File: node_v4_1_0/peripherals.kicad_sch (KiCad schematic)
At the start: 28 parts, among them J3 Conn_Coaxial, U10 MCP7940 / DS1307 / PCF8523, U11 1042240820, U12 CAT24M01W, U13 MAX31342EWA+T, U6 RFM69HCW, U9 SIM7080G

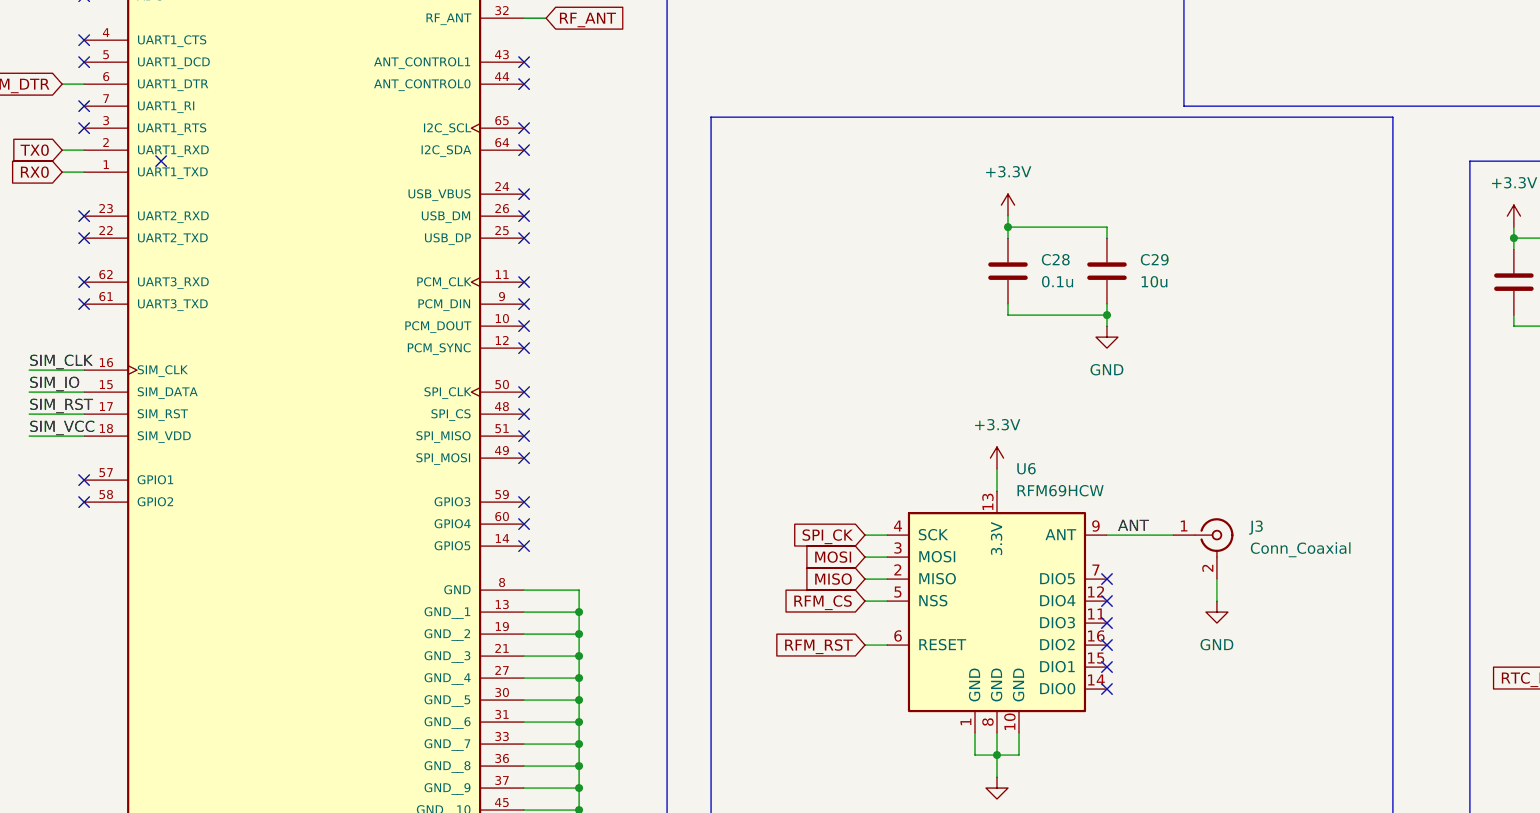
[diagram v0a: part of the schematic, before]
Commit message: small changes to 4.1.1 routing
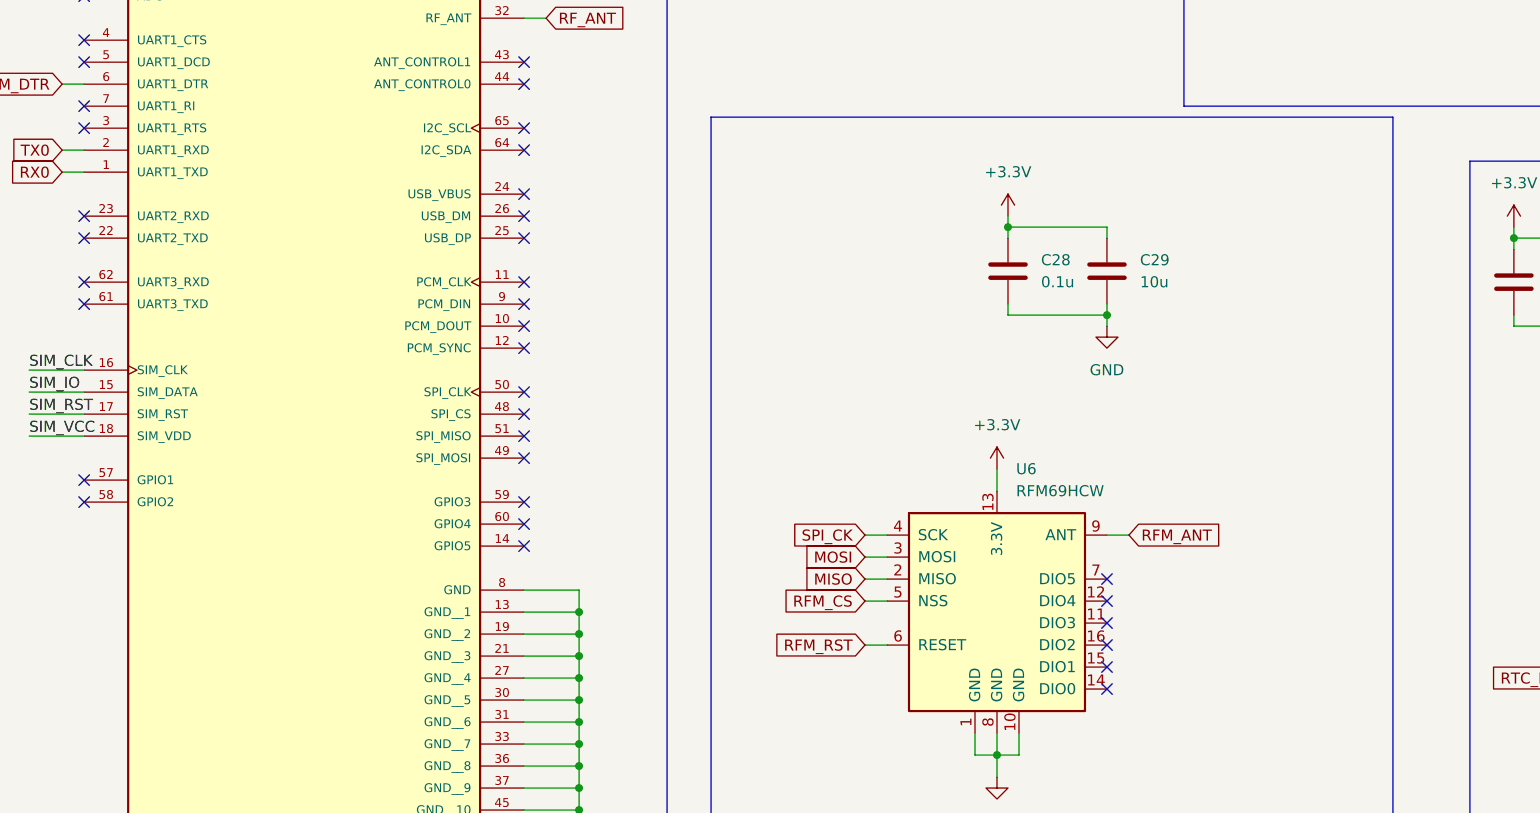
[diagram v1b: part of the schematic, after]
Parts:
- removed J3: Conn_Coaxial, Connector_Coaxial:SMA_Samtec_SMA-J-P-H-ST-EM1_EdgeMount, symbol Connector:Conn_Coaxial
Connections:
- net ANT renamed RFM_ANT
- no-connect marks 42 -> 41
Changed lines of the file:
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@@
 	)
 	(no_connect
-		(at 44.45 73.66)
-	)
-	(no_connect
 		(at 86.36 49.53)
 	)
@@
 	(wire
 		(pts
-			(xy 166.37 121.92) (xy 166.37 124.46)
+			(xy 86.36 146.05) (xy 92.71 146.05)
 		)
 		(stroke
@@
 	(wire
 		(pts
-			(xy 86.36 146.05) (xy 92.71 146.05)
+			(xy 260.35 96.52) (xy 261.62 96.52)
 		)
 		(stroke
@@
 	(wire
 		(pts
-			(xy 260.35 96.52) (xy 261.62 96.52)
+			(xy 160.02 179.07) (xy 171.45 179.07)
 		)
 		(stroke
@@
 	(wire
 		(pts
-			(xy 160.02 179.07) (xy 171.45 179.07)
+			(xy 115.57 166.37) (xy 115.57 167.64)
 		)
 		(stroke
@@
 	(wire
 		(pts
-			(xy 115.57 166.37) (xy 115.57 167.64)
+			(xy 153.67 116.84) (xy 156.21 116.84)
 		)
 		(stroke
@@
 	(wire
 		(pts
-			(xy 153.67 116.84) (xy 161.29 116.84)
-		)
-		(stroke
-			(width 0)
-			(type default)
-		)
-	)
-	(wire
-		(pts
 			(xy 92.71 176.53) (xy 92.71 173.99)
 		)
@@
 		)
 	)
-	(label "ANT"
-		(at 154.94 116.84 0)
-		(fields_autoplaced yes)
-		(effects
-			(font
-				(size 1.27 1.27)
-			)
-			(justify left bottom)
-		)
-	)
 	(label "RTC_X2"
 		(at 238.76 133.35 180)
@@
 		)
 	)
+	(global_label "RFM_ANT"
+		(shape input)
+		(at 156.21 116.84 0)
+		(fields_autoplaced yes)
+		(effects
+			(font
+				(size 1.27 1.27)
+			)
+			(justify left)
+		)
+		(property "Intersheetrefs" "${INTERSHEET_REFS}"
+			(at 167.3595 116.84 0)
+			(effects
+				(font
+					(size 1.27 1.27)
+				)
+				(justify left)
+				(hide yes)
+			)
+		)
+	)
 	(global_label "SDA"
 		(shape input)
@@
 	)
 	(symbol
-		(lib_id "power:GND")
-		(at 166.37 124.46 0)
-		(unit 1)
-		(exclude_from_sim no)
-		(in_bom yes)
-		(on_board yes)
-		(dnp no)
-		(fields_autoplaced yes)
-		(property "Reference" "#PWR045"
-			(at 166.37 130.81 0)
-			(effects
-				(font
-					(size 1.27 1.27)
-				)
-				(hide yes)
-			)
-		)
-		(property "Value" "GND"
-			(at 166.37 129.54 0)
-			(effects
-				(font
-					(size 1.27 1.27)
-				)
-			)
-		)
-		(property "Footprint" ""
-			(at 166.37 124.46 0)
-			(effects
-				(font
-					(size 1.27 1.27)
-				)
-				(hide yes)
-			)
-		)
-		(property "Datasheet" ""
-			(at 166.37 124.46 0)
-			(effects
-				(font
-					(size 1.27 1.27)
-				)
-				(hide yes)
-			)
-		)
-		(property "Description" "Power symbol creates a global label with name \"GND\" , ground"
-			(at 166.37 124.46 0)
-			(effects
-				(font
-					(size 1.27 1.27)
-				)
-				(hide yes)
-			)
-		)
-		(pin "1"
-		)
-		(instances
-			(project "node_v4_0"
-				(path "/03dc898e-8f05-4377-b5c6-8a0f09836da8/5fbf5ca9-9545-4205-a66a-787da56b16b9"
-					(reference "#PWR045")
-					(unit 1)
-				)
-			)
-		)
-	)
-	(symbol
 		(lib_id "Device:R")
 		(at 111.76 173.99 0)
@@
 					(unit 1)
 				)
-			)
-		)
-	)
-	(symbol
-		(lib_id "Connector:Conn_Coaxial")
-		(at 166.37 116.84 0)
-		(unit 1)
-		(exclude_from_sim no)
-		(in_bom yes)
-		(on_board yes)
-		(dnp no)
-		(fields_autoplaced yes)
-		(property "Reference" "J3"
-			(at 170.18 115.8631 0)
-			(effects
-				(font
-					(size 1.27 1.27)
-				)
-				(justify left)
-			)
-		)
-		(property "Value" "Conn_Coaxial"
-			(at 170.18 118.4031 0)
-			(effects
-				(font
-					(size 1.27 1.27)
-				)
-				(justify left)
-			)
-		)
-		(property "Footprint" "Connector_Coaxial:SMA_Samtec_SMA-J-P-H-ST-EM1_EdgeMount"
-			(at 166.37 116.84 0)
-			(effects
-				(font
-					(size 1.27 1.27)
-				)
-				(hide yes)
-			)
-		)
-		(property "Datasheet" "~"
-			(at 166.37 116.84 0)
-			(effects
-				(font
-					(size 1.27 1.27)
-				)
-				(hide yes)
-			)
-		)
-		(property "Description" "coaxial connector (BNC, SMA, SMB, SMC, Cinch/RCA, LEMO, ...)"
-			(at 166.37 116.84 0)
-			(effects
-				(font
-					(size 1.27 1.27)
-				)
-				(hide yes)
-			)
-		)
-		(pin "2"
-		)
-		(pin "1"
-		)
-		(instances
-			(project ""
-				(path "/03dc898e-8f05-4377-b5c6-8a0f09836da8/5fbf5ca9-9545-4205-a66a-787da56b16b9"
-					(reference "J3")
-					(unit 1)
-				)
